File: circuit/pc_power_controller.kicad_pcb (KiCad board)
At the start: 2 copper layers, 95 x 72 mm, 7 parts, among them J1 PWR_SW_HEADER, J2 PLED_HEADER, U1 TLP225A(F), U2 TLP621-1, U3 Seeed_XIAO_ESP32C3

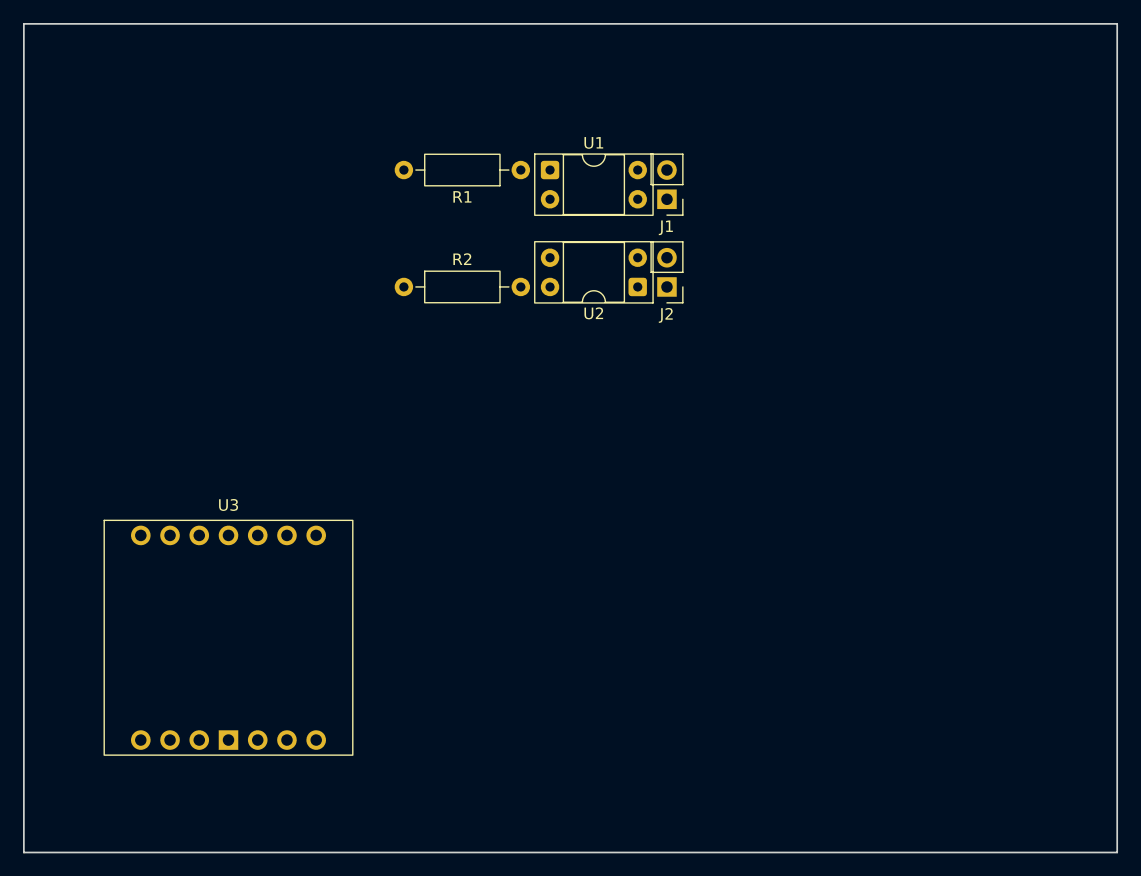
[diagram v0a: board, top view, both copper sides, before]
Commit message: fix: correct XIAO pin mapping, clean up schematic wiring, add ESPHome firmware
- Fix Seeed XIAO ESP32C3 pad/pin mapping in schematic symbol, footprint,
  and PCB net assignment (5V/GND/3V3 physically sit at the end of the
  right pin column, not the start of the left column as first assumed).
- Rewrite schematic wiring to use net labels for all inter-component
  signals instead of long routed wires across the page; fixes a real bug
  where a 3V3 wire crossed through the GPIO_MON label stub and merged
  the two nets.
- Add ESPHome firmware (esphome/) for the XIAO ESP32C3: momentary PWR_SW
  pulse button, separate forced-power-off button/script, and PLED
  blink/on/off detection via a single gpio binary_sensor (pulse_counter
  was removed since ESPHome can't share one pin across two components).

Co-Authored-By: Claude Sonnet 5 <noreply@anthropic.com>
Claude-Session: https://claude.ai/code/session_017SHrsAt73jUX19kpfbZs3f
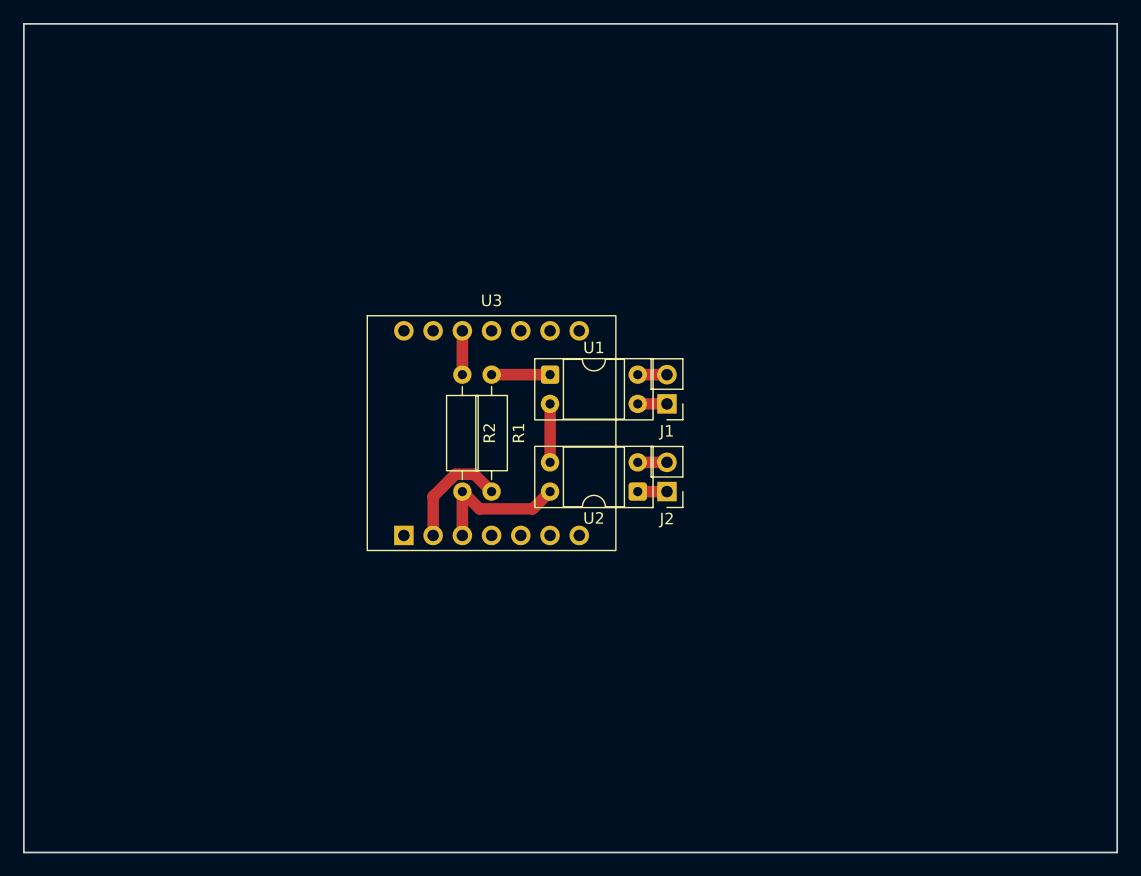
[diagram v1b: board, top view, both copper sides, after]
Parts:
- moved U3 29.0 mm to (50.8, 45.7)
- moved R1 18.0 mm to (50.8, 40.6), turned to -90 degrees
- moved J1 17.8 mm to (66.0, 43.2)
- moved U1 17.8 mm to (55.9, 40.6)
- moved J2 17.8 mm to (66.0, 50.8)
- moved U2 17.8 mm to (63.5, 50.8)
- moved R2 9.16 mm to (48.3, 40.6), turned to -90 degrees
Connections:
- U3 pad 12: (no net) -> 3V3
- U3 pad 13: (no net) -> GND
- U3 pad 2: GND -> GPIO_CTRL
- U3 pad 3: 3V3 -> GPIO_MON
- U3 pad 5: GPIO_CTRL -> (no net)
- U3 pad 6: GPIO_MON -> (no net)
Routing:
- net GPIO_MON: track 0.00 -> 12.7 mm
- net GPIO_CTRL: track 0.00 -> 9.89 mm
- net GND: track 0.00 -> 5.08 mm
- net R1_U1: track 0.00 -> 5.08 mm
- net 3V3: track 0.00 -> 3.81 mm
- net PWR_SW_B: track 0.00 -> 2.54 mm
- net PWR_SW_A: track 0.00 -> 2.54 mm
- net PLED_B: track 0.00 -> 2.54 mm
- net PLED_A: track 0.00 -> 2.54 mm
